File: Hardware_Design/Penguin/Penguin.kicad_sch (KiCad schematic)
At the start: 19 parts, among them J1 USB_B_Micro, SW1 SW_SPDT, U1 STM32F405RGT6, Y2 25 MHz

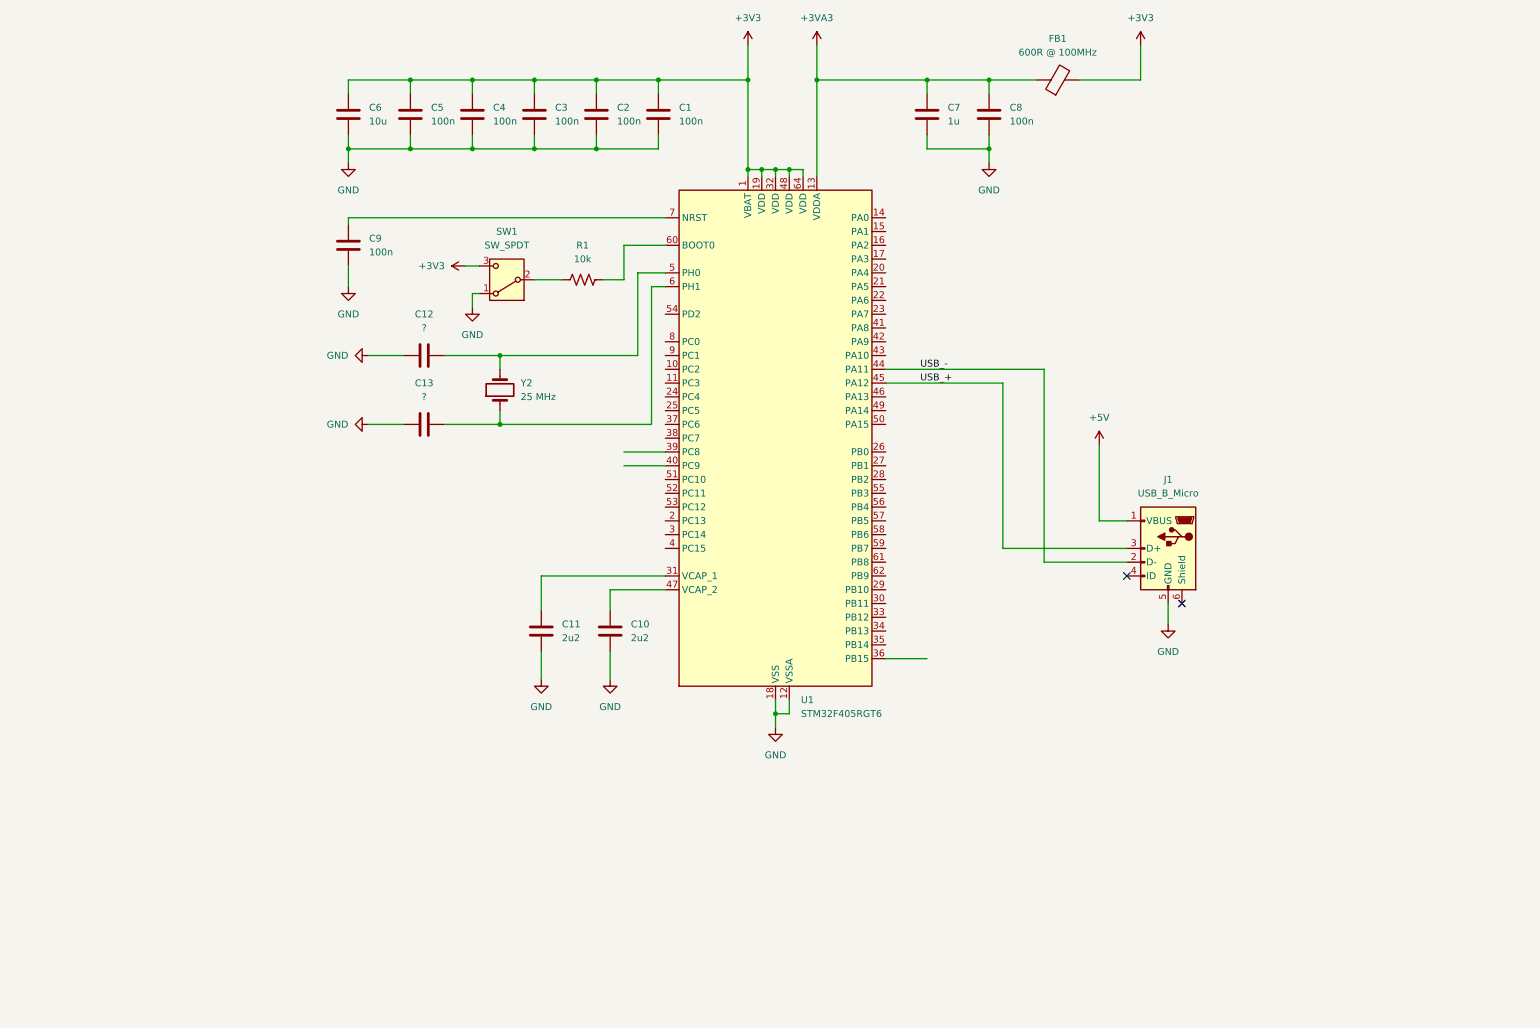
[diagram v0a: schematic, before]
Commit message: Added IMU, Mag, Alt
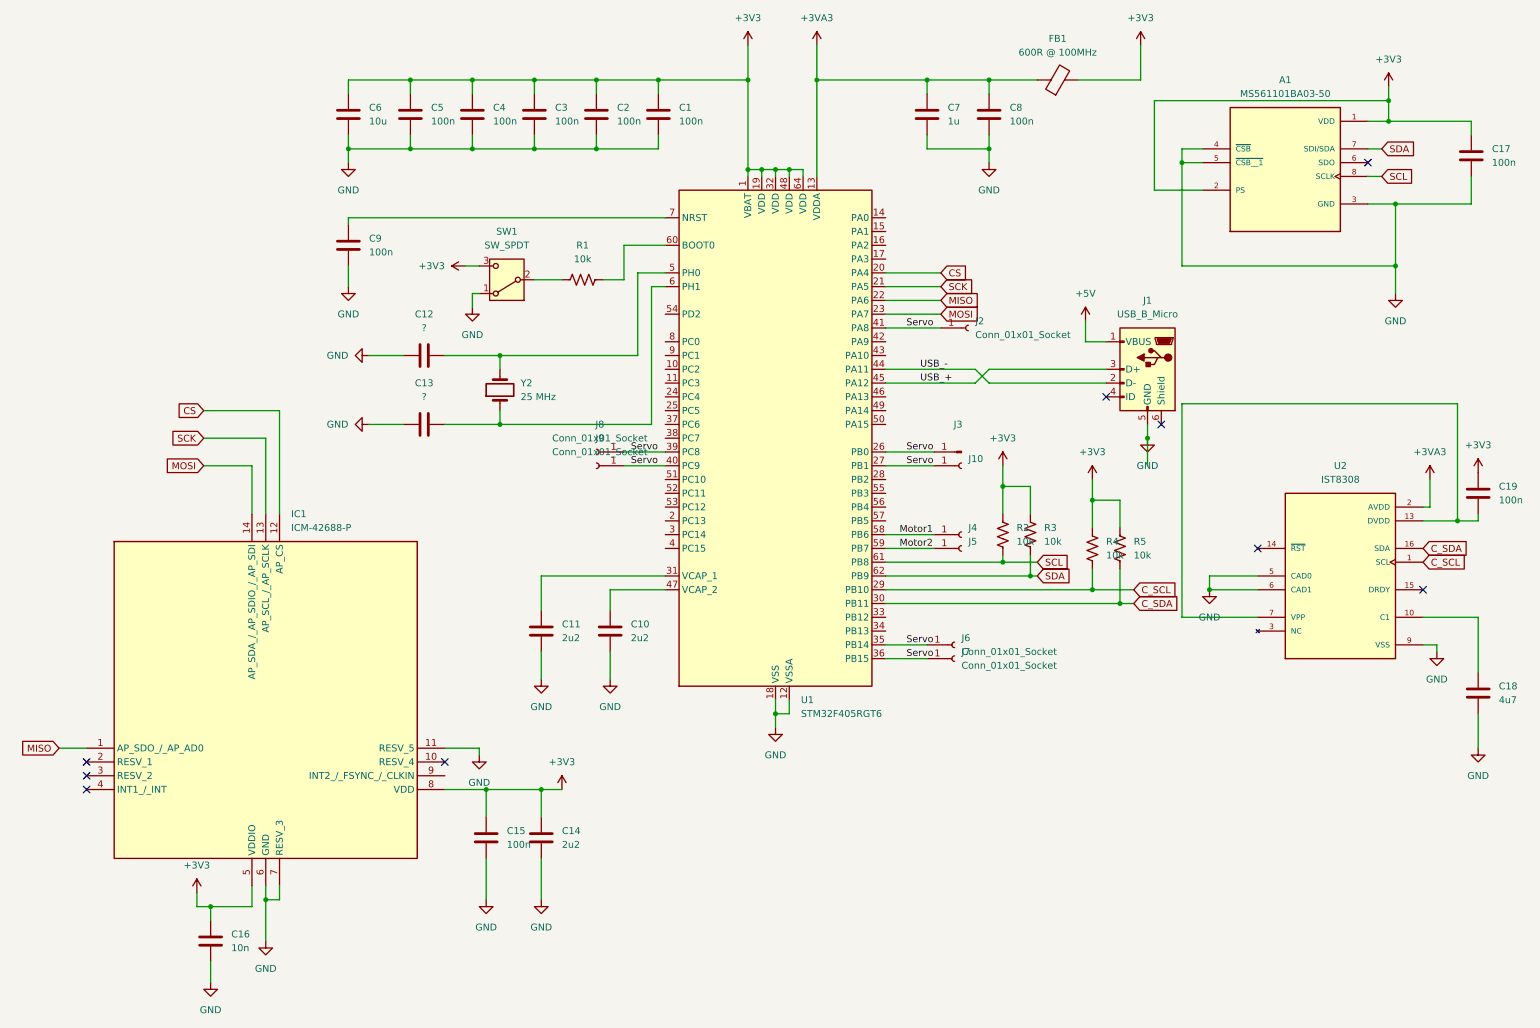
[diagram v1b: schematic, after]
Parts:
- added A1: MS561101BA03-50, MS561101BA03-50:XDCR_MS561101BA03-50, symbol MS5611:MS561101BA03-50
- added C14: 2u2, symbol Device:C
- added C15, C17, C19: 100n, symbol Device:C
- added C16: 10n, symbol Device:C
- added C18: 4u7, symbol Device:C
- added IC1: ICM-42688-P, IIM42352, symbol ICM42688:ICM-42688-P
- added J10, J2, J4, J5, J6, J7, J8, J9: Conn_01x01_Socket, symbol Connector:Conn_01x01_Socket
- added J3: Conn_01x01_Pin, symbol Connector:Conn_01x01_Pin
- added R2, R3, R4, R5: 10k, symbol Device:R_US
- added U2: IST8308, IST8308:PQFN50P300X300X110-16N, symbol iST8308:IST8308
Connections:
- net +3V3: now also A1.1 (VDD), A1.2 (PS), C14.1, C15.1, C16.1, C17.1, C19.1, IC1.5 (VDDIO), IC1.8 (VDD), R2.1, R3.1, R4.1, R5.1
- net +3VA3: now also U2.2 (AVDD)
- net GND: now also A1.3 (GND), A1.4 (~{CSB}), A1.5 (~{CSB__1}), C14.2, C15.2, C16.2, C17.2, C18.2, IC1.11 (RESV_5), IC1.6 (GND), IC1.7 (RESV_3), U2.11 (VSS), U2.5 (CAD0), U2.6 (CAD1), U2.9 (VSS)
- net CS: now reaches U1.20 (PA4)
- net CS: now also IC1.12 (AP_CS)
- net SCK: now reaches U1.21 (PA5)
- net SCK: now also IC1.13 (AP_SCL_/_AP_SCLK)
- net MISO: now reaches U1.22 (PA6)
- net MISO: now also IC1.1 (AP_SDO_/_AP_AD0)
- net MOSI: now reaches U1.23 (PA7)
- net MOSI: now also IC1.14 (AP_SDA_/_AP_SDIO_/_AP_SDI)
- net Servo: now reaches U1.26 (PB0)
- net Servo: now also U1.27 (PB1), U1.35 (PB14), U1.36 (PB15), U1.39 (PC8), U1.40 (PC9), U1.41 (PA8), J10.1 (Pin_1), J2.1 (Pin_1), J3.1 (Pin_1), J6.1 (Pin_1), J7.1 (Pin_1), J8.1 (Pin_1), J9.1 (Pin_1)
- net C_SCL: now reaches U1.29 (PB10)
- net C_SCL: now also R4.2, U2.1 (SCL)
- net C_SDA: now reaches U1.30 (PB11)
- net C_SDA: now also R5.2, U2.16 (SDA)
- net Motor1: now reaches U1.58 (PB6)
- net Motor1: now also J4.1 (Pin_1)
- net Motor2: now reaches U1.59 (PB7)
- net Motor2: now also J5.1 (Pin_1)
- net SCL: now reaches U1.61 (PB8)
- net SCL: now also A1.8 (SCLK), R2.2
- net SDA: now reaches U1.62 (PB9)
- net SDA: now also A1.7 (SDI/SDA), R3.2
- new net: C18.1, U2.10 (C1)
- new net: U2.12 (NC), U2.3 (NC), U2.4 (NC), U2.8 (NC)
- new net: C19.2, U2.13 (DVDD), U2.7 (VPP)
- no-connect marks 2 -> 9
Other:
- moved on the sheet: J1
